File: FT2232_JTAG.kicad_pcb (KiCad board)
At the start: 2 copper layers, 36.6 x 24 mm, 39 parts, among them J1 USB_C_Receptacle_USB2.0_16P, J2 Conn_01x09, J3 Conn_01x06, U1 FT2232HQ, U2 93LCxxB, U3 MCP1700x-330xxTT, Y1 12.000 MHz

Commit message: wip
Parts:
- added H1: MountingHole, MountingHole:MountingHole_2.2mm_M2_ISO14580, F.Cu at (74.2, 90.8)
- added H2: MountingHole, MountingHole:MountingHole_2.2mm_M2_ISO14580, F.Cu at (105.2, 109.2)
- added H3: MountingHole, MountingHole:MountingHole_2.2mm_M2_ISO14580, F.Cu at (74.2, 109.2)
- added H4: MountingHole, MountingHole:MountingHole_2.2mm_M2_ISO14580, F.Cu at (105.2, 90.8)
- moved C19 17.7 mm to (85.9, 102.5), turned to -90 degrees
- moved C18 15.6 mm to (84.9, 102.5), turned to -90 degrees
- moved L2 13.4 mm to (83.9, 102.5), turned to 90 degrees
- moved C17 13.4 mm to (82.9, 102.5), turned to 90 degrees
- moved L1 9.55 mm to (83.9, 100.3), turned to 90 degrees
- moved C14 9.45 mm to (82.9, 100.3), turned to 90 degrees
- moved C15 7.84 mm to (84.9, 100.3), turned to -90 degrees
- moved C16 6.46 mm to (85.9, 100.3), turned to -90 degrees
- moved R11 5.49 mm to (100.8, 104.2), turned to -90 degrees
- moved C12 4.95 mm to (82.2, 104.6), turned to 90 degrees
- moved R6 4.67 mm to (97.2, 94.2)
- moved C11 4.56 mm to (86.6, 104.6), turned to 90 degrees
- moved R3 4.43 mm to (88.0, 90.8), turned to 180 degrees
- moved J2 4.40 mm to (85.0, 109.2)
- moved U3 0.82 mm to (84.4, 105.6), turned to -90 degrees
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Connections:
- net Net-(U1-DM) renamed /D-
- net Net-(U1-DP) renamed /D+
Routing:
- net +3.3VP: track 0.00 -> 22.9 mm
- net +3.3V: track 0.00 -> 13.9 mm, vias 0 -> 5
- net /CLK: track 0.00 -> 8.56 mm
- net /TMS: track 0.00 -> 8.29 mm
- net /HOLD: track 0.00 -> 8.06 mm
- net /TCK: track 0.00 -> 6.89 mm
- net /TDO: track 0.00 -> 6.57 mm
- net /CDONE: track 0.00 -> 6.56 mm
- net /MOSI: track 0.00 -> 6.50 mm
- net /TDI: track 0.00 -> 5.85 mm
- net /CRESET_B: track 0.00 -> 5.83 mm
- net Net-(U1-EECS): track 0.00 -> 5.47 mm
- net /SS: track 0.00 -> 5.43 mm
- net /MISO: track 0.00 -> 5.06 mm
- net +1V8: track 1.47 -> 5.56 mm
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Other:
- outline, holes or cut-outs redrawn
- board text added: "GND"
- board text added: "TCK"
- board text added: "TDI"
- board text added: "TDO"
- board text added: "TMS"
- board text added: "VCC"

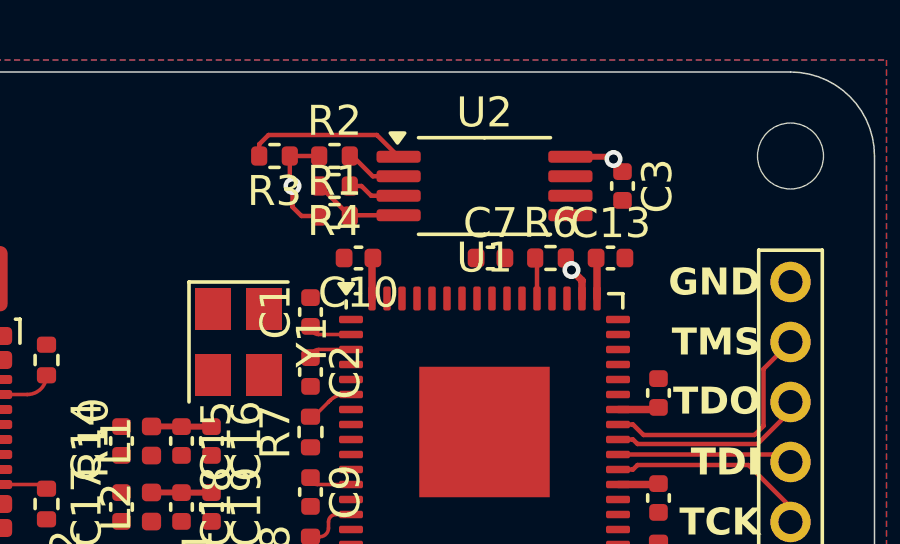
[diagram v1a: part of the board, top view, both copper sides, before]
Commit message: Fixed pull on BCBUS7
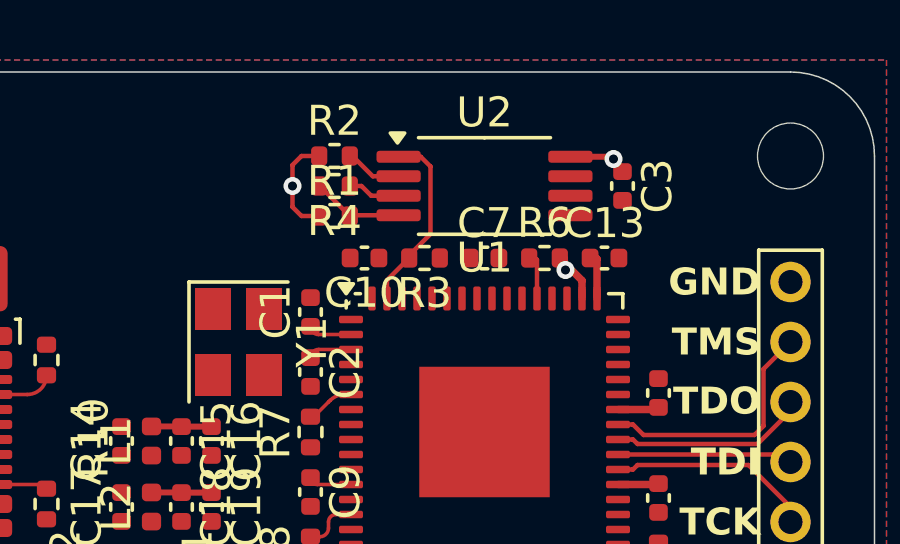
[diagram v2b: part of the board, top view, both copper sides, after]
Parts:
- moved R3 6.05 mm to (93.0, 94.2)
- moved C10 0.20 mm to (91.0, 94.2)
- moved C13 0.20 mm to (99.0, 94.2)
- moved C7 0.20 mm to (95.0, 94.2)
- moved R6 0.20 mm to (97.0, 94.2)
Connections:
- R11 pad 1: Net-(U1-BCBUS7) -> GND
- U1 pad 59: Net-(U1-BCBUS7) -> +3.3VP
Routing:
- net +1V8: track 5.56 -> 4.20 mm
- net Net-(U1-EECS): track 5.47 -> 6.20 mm
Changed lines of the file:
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@@
 	(net 55 "VPLL")
 	(net 56 "+3.3VP")
-	(net 57 "Net-(U1-BCBUS7)")
 	(footprint "Crystal:Crystal_SMD_3225-4Pin_3.2x2.5mm"
 		(layer "F.Cu")
@@
 	(footprint "Capacitor_SMD:C_0402_1005Metric"
 		(layer "F.Cu")
-		(at 99.2 94.2)
+		(at 99 94.2)
 		(descr "Capacitor SMD 0402 (1005 Metric), square (rectangular) end terminal, IPC_7351 nominal, (Body size source: IPC-SM-782 page 76, https://www.pcb-3d.com/wordpress/wp-content/uploads/ipc-sm-782a_amendment_1_and_2.pdf), generated with kicad-footprint-generator")
 		(tags "capacitor")
@@
 	(footprint "Capacitor_SMD:C_0402_1005Metric"
 		(layer "F.Cu")
-		(at 95.2 94.2)
+		(at 95 94.2)
 		(descr "Capacitor SMD 0402 (1005 Metric), square (rectangular) end terminal, IPC_7351 nominal, (Body size source: IPC-SM-782 page 76, https://www.pcb-3d.com/wordpress/wp-content/uploads/ipc-sm-782a_amendment_1_and_2.pdf), generated with kicad-footprint-generator")
 		(tags "capacitor")
@@
 		(tags "resistor")
 		(property "Reference" "R4"
-			(at 0 -1.17 0)
+			(at 0 -1.17 360)
 			(layer "F.SilkS")
 			(effects
@@
 		)
 		(property "Value" "2k"
-			(at 0 1.17 0)
+			(at 0 1.17 360)
 			(layer "F.Fab")
 			(effects
@@
 		)
 		(fp_text user "${REFERENCE}"
-			(at 0 0 0)
+			(at 0 0 360)
 			(layer "F.Fab")
 			(effects
@@
 		(tags "USB 2.0 C Type-C Receptacle SMD 16P 16C USB4110-GF-A")
 		(property "Reference" "J1"
-			(at 0 -5.015 270)
+			(at 0 -5.015 -90)
 			(unlocked yes)
 			(layer "F.SilkS")
@@
 	(footprint "Capacitor_SMD:C_0402_1005Metric"
 		(layer "F.Cu")
-		(at 90.8 94.2 180)
+		(at 91 94.2 180)
 		(descr "Capacitor SMD 0402 (1005 Metric), square (rectangular) end terminal, IPC_7351 nominal, (Body size source: IPC-SM-782 page 76, https://www.pcb-3d.com/wordpress/wp-content/uploads/ipc-sm-782a_amendment_1_and_2.pdf), generated with kicad-footprint-generator")
 		(tags "capacitor")
@@
 	(footprint "Resistor_SMD:R_0402_1005Metric"
 		(layer "F.Cu")
-		(at 97.2 94.2)
+		(at 97 94.2)
 		(descr "Resistor SMD 0402 (1005 Metric), square (rectangular) end terminal, IPC_7351 nominal, (Body size source: IPC-SM-782 page 72, https://www.pcb-3d.com/wordpress/wp-content/uploads/ipc-sm-782a_amendment_1_and_2.pdf), generated with kicad-footprint-generator")
 		(tags "resistor")
@@
 		(tags "resistor")
 		(property "Reference" "R2"
-			(at 0 -1.17 0)
+			(at 0 -1.17 360)
 			(layer "F.SilkS")
 			(effects
@@
 		)
 		(property "Value" "10k"
-			(at 0 1.17 0)
+			(at 0 1.17 360)
 			(layer "F.Fab")
 			(effects
@@
 		)
 		(fp_text user "${REFERENCE}"
-			(at 0 0 0)
+			(at 0 0 360)
 			(layer "F.Fab")
 			(effects
@@
 			(layers "F.Cu" "F.Paste" "F.Mask")
 			(roundrect_rratio 0.25)
-			(net 57 "Net-(U1-BCBUS7)")
+			(net 37 "GND")
 			(pintype "passive")
 		)
@@
 	(footprint "Resistor_SMD:R_0402_1005Metric"
 		(layer "F.Cu")
-		(at 88 90.8 180)
+		(at 93 94.2 180)
 		(descr "Resistor SMD 0402 (1005 Metric), square (rectangular) end terminal, IPC_7351 nominal, (Body size source: IPC-SM-782 page 72, https://www.pcb-3d.com/wordpress/wp-content/uploads/ipc-sm-782a_amendment_1_and_2.pdf), generated with kicad-footprint-generator")
 		(tags "resistor")
 		(property "Reference" "R3"
-			(at 0 -1.17 0)
+			(at 0 -1.17 360)
 			(layer "F.SilkS")
 			(effects
@@
 		)
 		(property "Value" "10k"
-			(at 0 1.17 0)
+			(at 0 1.17 360)
 			(layer "F.Fab")
 			(effects
@@
 		)
 		(fp_text user "${REFERENCE}"
-			(at 0 0 0)
+			(at 0 0 360)
 			(layer "F.Fab")
 			(effects
@@
 		(tags "TSSOP SO")
 		(property "Reference" "U2"
-			(at 0 -2.45 0)
+			(at 0 -2.45 360)
 			(layer "F.SilkS")
 			(effects
@@
 		)
 		(property "Value" "93LCxxB"
-			(at 0 2.45 0)
+			(at 0 2.45 360)
 			(layer "F.Fab")
 			(effects
@@
 		)
 		(fp_text user "${REFERENCE}"
-			(at 0 0 0)
+			(at 0 0 360)
 			(layer "F.Fab")
 			(effects
@@
 		(tags "resistor")
 		(property "Reference" "R1"
-			(at 0 -1.17 0)
+			(at 0 -1.17 360)
 			(layer "F.SilkS")
 			(effects
@@
 		)
 		(property "Value" "10k"
-			(at 0 1.17 0)
+			(at 0 1.17 360)
 			(layer "F.Fab")
 			(effects
@@
 		)
 		(fp_text user "${REFERENCE}"
-			(at 0 0 0)
+			(at 0 0 360)
 			(layer "F.Fab")
 			(effects
@@
 			(layers "F.Cu" "F.Paste" "F.Mask")
 			(roundrect_rratio 0.25)
-			(net 57 "Net-(U1-BCBUS7)")
+			(net 56 "+3.3VP")
 			(pinfunction "BCBUS7")
 			(pintype "bidirectional")
@@
 	)
 	(segment
-		(start 91.25 95.55)
-		(end 91.25 94.23)
-		(width 0.25)
-		(layer "F.Cu")
-		(net 6)
-	)
-	(segment
-		(start 91.25 94.23)
-		(end 91.28 94.2)
-		(width 0.25)
-		(layer "F.Cu")
-		(net 6)
-	)
-	(segment
 		(start 98.75 95.55)
 		(end 98.75 94.23)
@@
 	)
 	(segment
-		(start 91.4125 90.1)
-		(end 87.8 90.1)
+		(start 93.2 93.4)
+		(end 93.2 91.150001)
+		(width 0.15)
+		(layer "F.Cu")
+		(net 33)
+	)
+	(segment
+		(start 91.75 95.55)
+		(end 91.75 94.94)
+		(width 0.15)
+		(layer "F.Cu")
+		(net 33)
+	)
+	(segment
+		(start 92.49 94.2)
+		(end 92.49 94.11)
 		(width 0.15)
 		(layer "F.Cu")
@@
 	)
 	(segment
-		(start 92.1375 90.825)
-		(end 91.4125 90.1)
+		(start 92.49 94.11)
+		(end 93.2 93.4)
 		(width 0.15)
 		(layer "F.Cu")
@@
 	)
 	(segment
-		(start 87.8 90.1)
-		(end 87.49 90.41)
+		(start 91.75 94.94)
+		(end 92.49 94.2)
 		(width 0.15)
 		(layer "F.Cu")
@@
 	)
 	(segment
-		(start 87.49 90.41)
-		(end 87.49 90.8)
+		(start 93.2 91.150001)
+		(end 92.874999 90.825)
+		(width 0.15)
+		(layer "F.Cu")
+		(net 33)
+	)
+	(segment
+		(start 92.874999 90.825)
+		(end 92.1375 90.825)
 		(width 0.15)
 		(layer "F.Cu")
@@
 	)
 	(segment
+		(start 88.9 90.8)
+		(end 89.49 90.8)
+		(width 0.15)
+		(layer "F.Cu")
+		(net 39)
+	)
+	(segment
 		(start 92.32 105.8)
 		(end 92.32 106.32)
@@
 	)
 	(segment
-		(start 89.49 90.8)
-		(end 88.51 90.8)
-		(width 0.15)
-		(layer "F.Cu")
-		(net 39)
-	)
-	(segment
 		(start 98.72 106.38)
 		(end 98.7 106.4)
@@
 	)
 	(segment
-		(start 88.51 90.8)
-		(end 88.51 91.71)
+		(start 88.6 91.1)
+		(end 88.9 90.8)
 		(width 0.15)
 		(layer "F.Cu")
@@
 	)
 	(segment
-		(start 88.6 90.89)
-		(end 88.51 90.8)
+		(start 88.6 91.8)
+		(end 88.6 91.1)
 		(width 0.15)
 		(layer "F.Cu")
@@
 	)
 	(segment
-		(start 88.51 91.71)
-		(end 88.6 91.8)
-		(width 0.15)
-		(layer "F.Cu")
-		(net 39)
-	)
-	(segment
 		(start 92.32 106.32)
 		(end 92.4 106.4)
@@
 	)
 	(via
-		(at 97.9 94.6)
+		(at 97.7 94.6)
 		(size 0.6)
 		(drill 0.3)

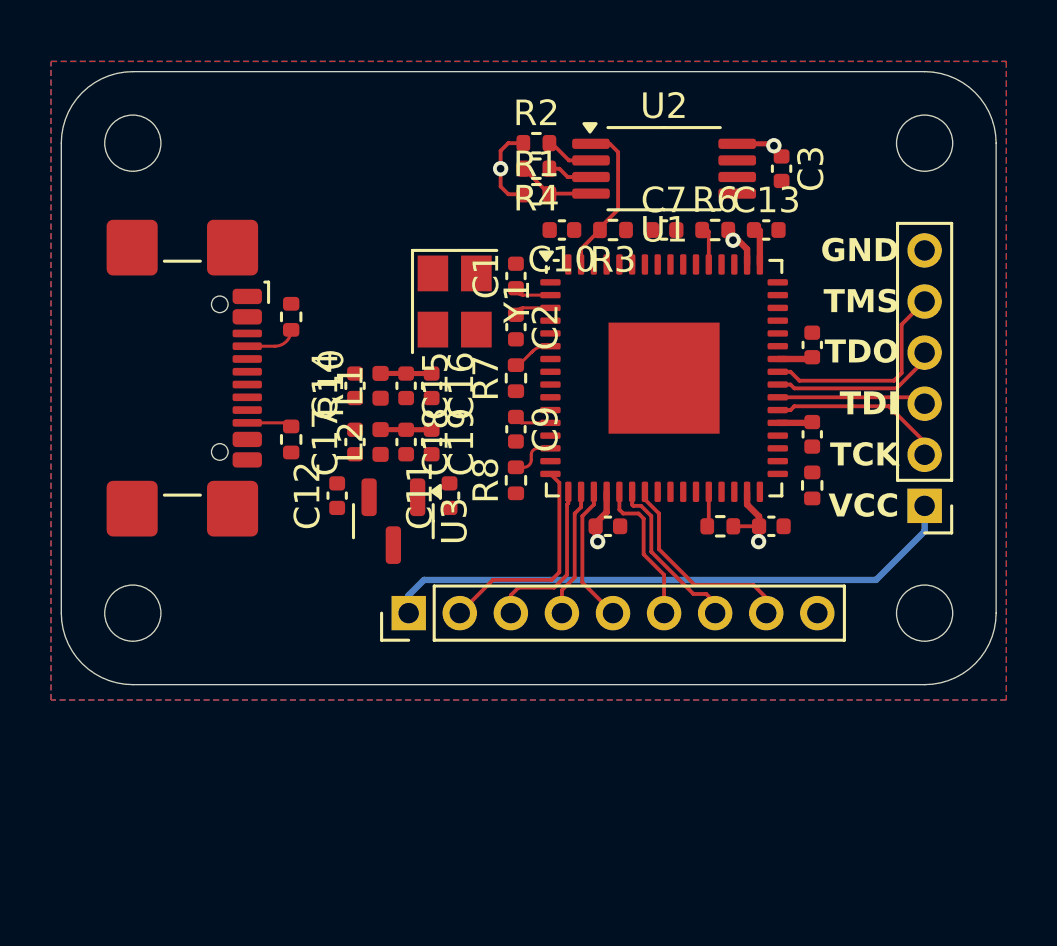
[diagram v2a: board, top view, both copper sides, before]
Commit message: Routing done. DRC ToDo.
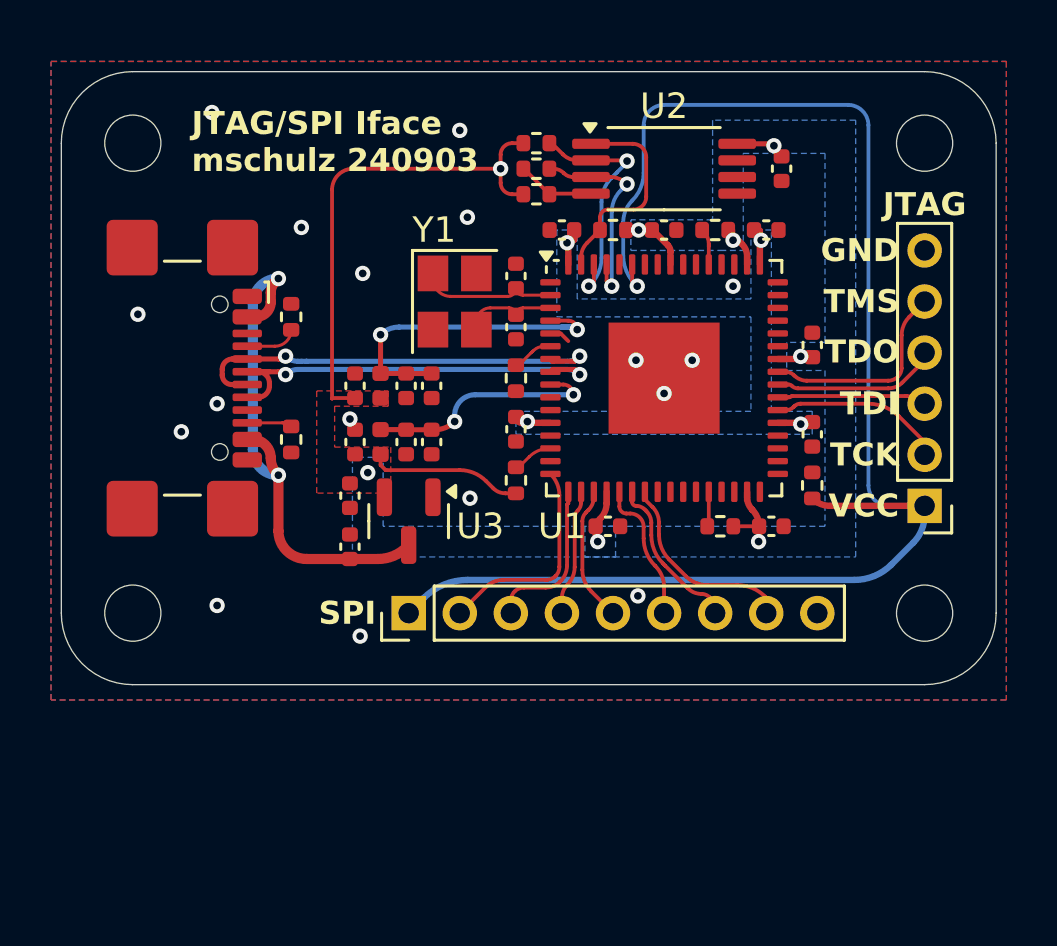
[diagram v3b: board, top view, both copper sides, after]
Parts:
- moved C11 4.38 mm to (82.7, 106.6)
- moved U3 0.60 mm to (85.0, 105.6)
- moved C12 0.50 mm to (82.7, 104.6), turned to -90 degrees
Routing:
- net +3.3VP: track 22.9 -> 60.7 mm, vias 0 -> 1
- net +3.3V: track 13.5 -> 38.2 mm, vias 5 -> 8
- net +5V: track 0.00 -> 21.1 mm, vias 0 -> 2
- net /D+: track 0.00 -> 17.8 mm, vias 0 -> 2
- net /D-: track 0.00 -> 17.0 mm, vias 0 -> 2
- net VPHY: track 2.00 -> 13.0 mm, vias 0 -> 2
- net Net-(U1-EECLK): track 1.91 -> 9.61 mm, vias 0 -> 2
- net VPLL: track 2.00 -> 9.42 mm, vias 0 -> 2
- net Net-(U1-EEDATA): track 1.76 -> 8.31 mm, vias 0 -> 2
- net Net-(U1-OSCI): track 1.49 -> 5.48 mm
- net Net-(U1-OSCO): track 1.49 -> 3.78 mm
- net Net-(U1-EECS): track 6.20 -> 8.34 mm
- net +1V8: track 4.20 -> 5.85 mm, vias 0 -> 4
- net GND: track 0.00 -> 0.82 mm, vias 0 -> 17
- added copper zone on B.Cu, net +1V8
- added copper zone on B.Cu, net +3.3V
- added copper zone on F.Cu, net +3.3V
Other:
- board text added: "JTAG"
- board text added: "JTAG/SPI Iface mschulz 240903"
- board text added: "SPI"
